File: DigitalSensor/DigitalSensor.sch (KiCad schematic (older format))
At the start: 0 parts

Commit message: Creating Digital Sensor Schematic
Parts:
- added C? (x2): CAP, symbol pspice:CAP
- added IC?: TTP223E-BA6, SOT95P285X126-6N, symbol TTP223E-BA6:TTP223E-BA6
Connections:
- new net GND: C?.2, C?.2, IC?.2 (VSS)
- new net Output: IC?.1 (Q)
- new net TouchPad: C?.1, IC?.3 (I)
- new net Vdd: C?.1, IC?.5 (VDD), IC?.6 (TOG)
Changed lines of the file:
@@
 Comment4 ""
 $EndDescr
+$Comp
+L TTP223E-BA6:TTP223E-BA6 IC?
+U 1 1 64037076
+P 5450 3750
+F 0 "IC?" H 6000 4015 50  0000 C CNN
+F 1 "TTP223E-BA6" H 6000 3924 50  0000 C CNN
+F 2 "SOT95P285X126-6N" H 6400 3850 50  0001 L CNN
+F 3 "https://datasheet.lcsc.com/szlcsc/1810251711_Tontek-Design-Tech-TTP223E-BA6_C129457.pdf" H 6400 3750 50  0001 L CNN
+F 4 "SOT-23-6 Touch Screen Controller ICs" H 6400 3650 50  0001 L CNN "Description"
+F 5 "1.26" H 6400 3550 50  0001 L CNN "Height"
+F 6 "Tontec" H 6400 3450 50  0001 L CNN "Manufacturer_Name"
+F 7 "TTP223E-BA6" H 6400 3350 50  0001 L CNN "Manufacturer_Part_Number"
+F 8 "" H 6400 3250 50  0001 L CNN "Mouser Part Number"
+F 9 "" H 6400 3150 50  0001 L CNN "Mouser Price/Stock"
+F 10 "" H 6400 3050 50  0001 L CNN "Arrow Part Number"
+F 11 "" H 6400 2950 50  0001 L CNN "Arrow Price/Stock"
+	1    5450 3750
+	1    0    0    -1
+$EndComp
+Text GLabel 4850 2700 0    50   Input ~ 0
+Vdd
+Wire Wire Line
+	4850 2700 6700 2700
+Wire Wire Line
+	6700 2700 6700 3750
+Wire Wire Line
+	6700 3750 6550 3750
+Connection ~ 6700 3750
+Wire Wire Line
+	6700 3750 6700 3850
+$Comp
+L pspice:CAP C?
+U 1 1 64038F20
+P 6700 4650
+F 0 "C?" H 6878 4696 50  0000 L CNN
+F 1 "CAP" H 6878 4605 50  0000 L CNN
+F 2 "" H 6700 4650 50  0001 C CNN
+F 3 "~" H 6700 4650 50  0001 C CNN
+	1    6700 4650
+	1    0    0    -1
+$EndComp
+Wire Wire Line
+	6550 3850 6700 3850
+Wire Wire Line
+	6700 4400 6700 3850
+Connection ~ 6700 3850
+Wire Wire Line
+	5100 4950 6700 4950
+Wire Wire Line
+	6700 4950 6700 4900
+$Comp
+L power:GND #PWR?
+U 1 1 6403A742
+P 5100 4950
+F 0 "#PWR?" H 5100 4700 50  0001 C CNN
+F 1 "GND" H 5105 4777 50  0000 C CNN
+F 2 "" H 5100 4950 50  0001 C CNN
+F 3 "" H 5100 4950 50  0001 C CNN
+	1    5100 4950
+	1    0    0    -1
+$EndComp
+Connection ~ 5100 4950
+Text GLabel 4000 3850 0    50   Input ~ 0
+TouchPad
+$Comp
+L pspice:CAP C?
+U 1 1 6403AB19
+P 4550 4100
+F 0 "C?" H 4728 4146 50  0000 L CNN
+F 1 "CAP" H 4728 4055 50  0000 L CNN
+F 2 "" H 4550 4100 50  0001 C CNN
+F 3 "~" H 4550 4100 50  0001 C CNN
+	1    4550 4100
+	1    0    0    -1
+$EndComp
+Wire Wire Line
+	4550 4350 4550 4700
+Wire Wire Line
+	4550 4700 5100 4700
+Wire Wire Line
+	5100 4700 5100 4950
+Wire Wire Line
+	5450 3850 5100 3850
+Wire Wire Line
+	5100 3850 5100 4700
+Connection ~ 5100 4700
+Wire Wire Line
+	5450 3950 5200 3950
+Wire Wire Line
+	5200 3950 5200 3650
+Wire Wire Line
+	4650 3650 4650 3850
+Wire Wire Line
+	4000 3850 4550 3850
+Wire Wire Line
+	4650 3650 5200 3650
+Connection ~ 4550 3850
+Wire Wire Line
+	4550 3850 4650 3850
+Text GLabel 4950 3350 0    50   Input ~ 0
+Output
+Wire Wire Line
+	4950 3350 5350 3350
+Wire Wire Line
+	5350 3350 5350 3750
+Wire Wire Line
+	5350 3750 5450 3750
 $EndSCHEMATC

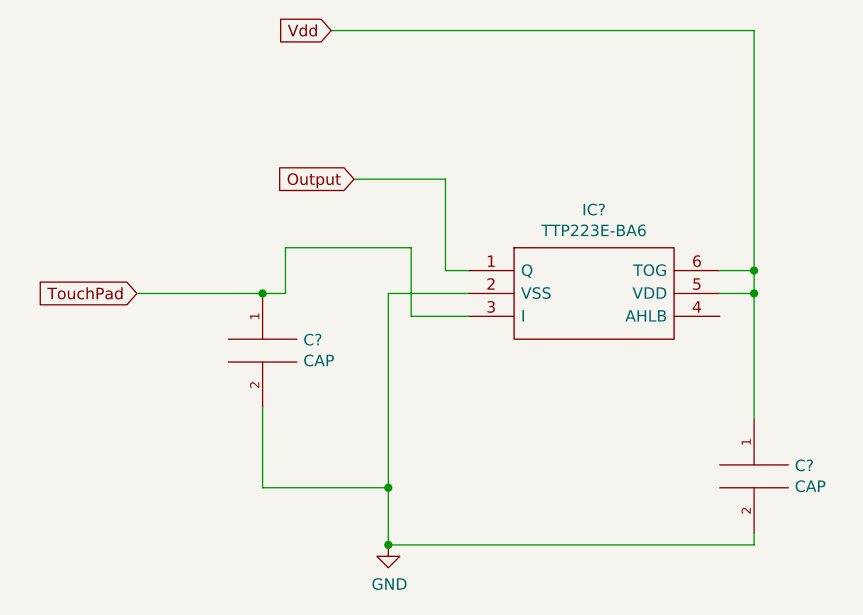
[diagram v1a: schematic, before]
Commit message: added component values
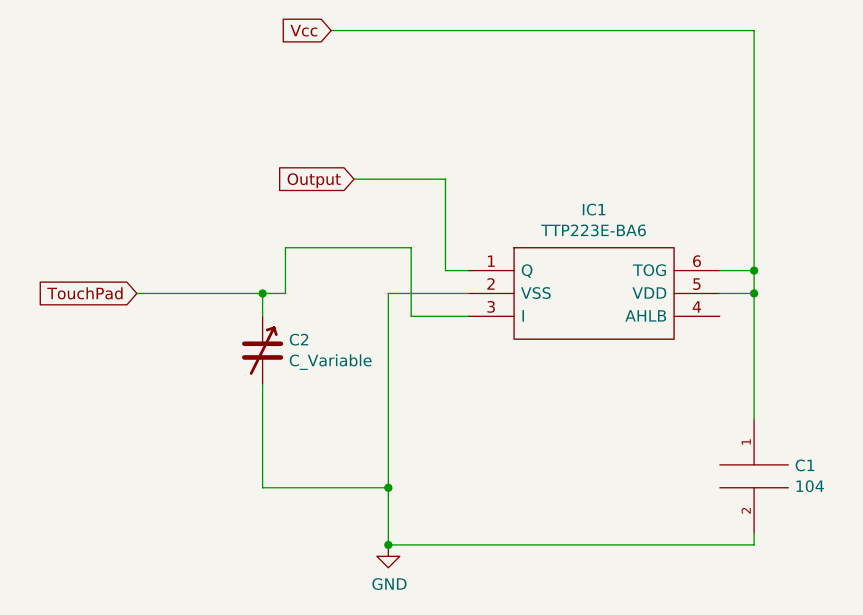
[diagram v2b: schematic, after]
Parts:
- removed C?: CAP, symbol pspice:CAP
- added C2: C_Variable, symbol Device:C_Variable
- C1: renamed from C?; value CAP -> 104; footprint (none) -> Capacitor_THT:CP_Axial_L10.0mm_D4.5mm_P15.00mm_Horizontal
- gave numbers to parts that had none: 1
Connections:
- net GND: now also C2.2
- net TouchPad: now also C2.1
- net Vdd renamed Vcc
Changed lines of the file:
@@
 $EndDescr
 $Comp
-L TTP223E-BA6:TTP223E-BA6 IC?
+L TTP223E-BA6:TTP223E-BA6 IC1
 U 1 1 64037076
 P 5450 3750
-F 0 "IC?" H 6000 4015 50  0000 C CNN
+F 0 "IC1" H 6000 4015 50  0000 C CNN
 F 1 "TTP223E-BA6" H 6000 3924 50  0000 C CNN
 F 2 "SOT95P285X126-6N" H 6400 3850 50  0001 L CNN
@@
 $EndComp
 Text GLabel 4850 2700 0    50   Input ~ 0
-Vdd
+Vcc
 Wire Wire Line
 	4850 2700 6700 2700
@@
 	6700 3750 6700 3850
 $Comp
-L pspice:CAP C?
+L pspice:CAP C1
 U 1 1 64038F20
 P 6700 4650
-F 0 "C?" H 6878 4696 50  0000 L CNN
-F 1 "CAP" H 6878 4605 50  0000 L CNN
-F 2 "" H 6700 4650 50  0001 C CNN
+F 0 "C1" H 6878 4696 50  0000 L CNN
+F 1 "104" H 6878 4605 50  0000 L CNN
+F 2 "Capacitor_THT:CP_Axial_L10.0mm_D4.5mm_P15.00mm_Horizontal" H 6700 4650 50  0001 C CNN
 F 3 "~" H 6700 4650 50  0001 C CNN
 	1    6700 4650
@@
 	6700 4950 6700 4900
 $Comp
-L power:GND #PWR?
+L power:GND #PWR0101
 U 1 1 6403A742
 P 5100 4950
-F 0 "#PWR?" H 5100 4700 50  0001 C CNN
+F 0 "#PWR0101" H 5100 4700 50  0001 C CNN
 F 1 "GND" H 5105 4777 50  0000 C CNN
 F 2 "" H 5100 4950 50  0001 C CNN
@@
 Text GLabel 4000 3850 0    50   Input ~ 0
 TouchPad
-$Comp
-L pspice:CAP C?
-U 1 1 6403AB19
-P 4550 4100
-F 0 "C?" H 4728 4146 50  0000 L CNN
-F 1 "CAP" H 4728 4055 50  0000 L CNN
-F 2 "" H 4550 4100 50  0001 C CNN
-F 3 "~" H 4550 4100 50  0001 C CNN
-	1    4550 4100
-	1    0    0    -1
-$EndComp
-Wire Wire Line
-	4550 4350 4550 4700
 Wire Wire Line
 	4550 4700 5100 4700
@@
 	4650 3650 4650 3850
 Wire Wire Line
-	4000 3850 4550 3850
-Wire Wire Line
 	4650 3650 5200 3650
-Connection ~ 4550 3850
-Wire Wire Line
-	4550 3850 4650 3850
 Text GLabel 4950 3350 0    50   Input ~ 0
 Output
@@
 Wire Wire Line
 	5350 3750 5450 3750
+$Comp
+L Device:C_Variable C2
+U 1 1 64049E25
+P 4550 4100
+F 0 "C2" H 4665 4146 50  0000 L CNN
+F 1 "C_Variable" H 4665 4055 50  0000 L CNN
+F 2 "" H 4550 4100 50  0001 C CNN
+F 3 "~" H 4550 4100 50  0001 C CNN
+	1    4550 4100
+	1    0    0    -1
+$EndComp
+Wire Wire Line
+	4000 3850 4550 3850
+Wire Wire Line
+	4550 3950 4550 3850
+Connection ~ 4550 3850
+Wire Wire Line
+	4550 3850 4650 3850
+Wire Wire Line
+	4550 4250 4550 4700
 $EndSCHEMATC

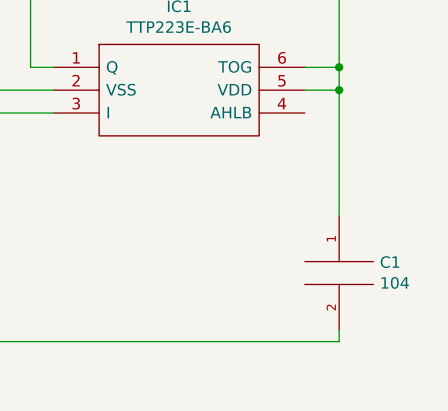
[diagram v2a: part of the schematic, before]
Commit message: finalising draft schematics
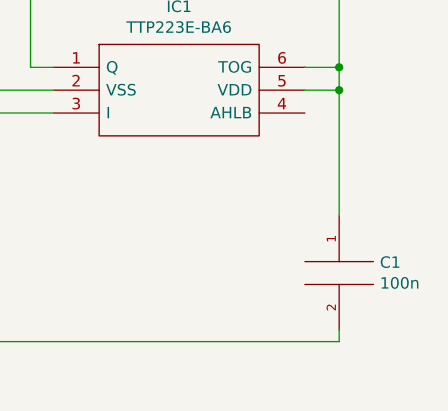
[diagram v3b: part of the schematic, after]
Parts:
- C1: value 104 -> 100n; Price (none) -> 0.0009
- C2: footprint (none) -> Capacitor_SMD:C_Trimmer_Murata_TZC3; Price (none) -> 0.3067
- IC1: footprint SOT95P285X126-6N -> TTP223E-BA6:SOT95P285X126-6N; Price (none) -> 0.1568
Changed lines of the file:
@@
 F 0 "IC1" H 6000 4015 50  0000 C CNN
 F 1 "TTP223E-BA6" H 6000 3924 50  0000 C CNN
-F 2 "SOT95P285X126-6N" H 6400 3850 50  0001 L CNN
+F 2 "TTP223E-BA6:SOT95P285X126-6N" H 6400 3850 50  0001 L CNN
 F 3 "https://datasheet.lcsc.com/szlcsc/1810251711_Tontek-Design-Tech-TTP223E-BA6_C129457.pdf" H 6400 3750 50  0001 L CNN
 F 4 "SOT-23-6 Touch Screen Controller ICs" H 6400 3650 50  0001 L CNN "Description"
@@
 F 10 "" H 6400 3050 50  0001 L CNN "Arrow Part Number"
 F 11 "" H 6400 2950 50  0001 L CNN "Arrow Price/Stock"
+F 12 "0.1568" H 5450 3750 50  0001 C CNN "Price"
 	1    5450 3750
 	1    0    0    -1
@@
 P 6700 4650
 F 0 "C1" H 6878 4696 50  0000 L CNN
-F 1 "104" H 6878 4605 50  0000 L CNN
+F 1 "100n" H 6878 4605 50  0000 L CNN
 F 2 "Capacitor_THT:CP_Axial_L10.0mm_D4.5mm_P15.00mm_Horizontal" H 6700 4650 50  0001 C CNN
 F 3 "~" H 6700 4650 50  0001 C CNN
+F 4 "0.0009" H 6700 4650 50  0001 C CNN "Price"
 	1    6700 4650
 	1    0    0    -1
@@
 F 0 "C2" H 4665 4146 50  0000 L CNN
 F 1 "C_Variable" H 4665 4055 50  0000 L CNN
-F 2 "" H 4550 4100 50  0001 C CNN
+F 2 "Capacitor_SMD:C_Trimmer_Murata_TZC3" H 4550 4100 50  0001 C CNN
 F 3 "~" H 4550 4100 50  0001 C CNN
+F 4 "0.3067" H 4550 4100 50  0001 C CNN "Price"
 	1    4550 4100
 	1    0    0    -1

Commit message: Updated schematics
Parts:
- IC1: JLCPCB Part # (none) -> C1693666; Manufacturer_Name Tontec -> Sam&wing; Manufacturer_Part_Number TTP223E-BA6 -> 223; Price 0.1568 -> 0.1
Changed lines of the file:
@@
 F 4 "SOT-23-6 Touch Screen Controller ICs" H 6400 3650 50  0001 L CNN "Description"
 F 5 "1.26" H 6400 3550 50  0001 L CNN "Height"
-F 6 "Tontec" H 6400 3450 50  0001 L CNN "Manufacturer_Name"
-F 7 "TTP223E-BA6" H 6400 3350 50  0001 L CNN "Manufacturer_Part_Number"
+F 6 "Sam&wing" H 6400 3450 50  0001 L CNN "Manufacturer_Name"
+F 7 "223" H 6400 3350 50  0001 L CNN "Manufacturer_Part_Number"
 F 8 "" H 6400 3250 50  0001 L CNN "Mouser Part Number"
 F 9 "" H 6400 3150 50  0001 L CNN "Mouser Price/Stock"
 F 10 "" H 6400 3050 50  0001 L CNN "Arrow Part Number"
 F 11 "" H 6400 2950 50  0001 L CNN "Arrow Price/Stock"
-F 12 "0.1568" H 5450 3750 50  0001 C CNN "Price"
+F 12 "0.1" H 5450 3750 50  0001 C CNN "Price"
+F 13 "C1693666" H 5450 3750 50  0001 C CNN "JLCPCB Part #"
 	1    5450 3750
 	1    0    0    -1
